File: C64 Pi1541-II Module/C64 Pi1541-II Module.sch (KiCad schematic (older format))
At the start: 28 parts, among them IC1 0.96_OLED, IC2 7406, IC3 I2C LC, J1 DC IN, J2 C64_IEC, J3 C64_IEC, J4 Faceplate, M1 Mounting, M2 Mounting, M3 Mounting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

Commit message: Changed dimensions on module
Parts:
- JP1, JP2: footprint Jumper:SolderJumper-3_P1.3mm_Open_RoundedPad1.0x1.5mm -> wire_pads:OLED_SEL
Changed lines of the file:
@@
 F 0 "JP2" V 8354 8768 50  0000 L CNN
 F 1 "P2_VCC" V 8445 8768 50  0000 L CNN
-F 2 "Jumper:SolderJumper-3_P1.3mm_Open_RoundedPad1.0x1.5mm" H 8400 8700 50  0001 C CNN
+F 2 "wire_pads:OLED_SEL" H 8400 8700 50  0001 C CNN
 F 3 "~" H 8400 8700 50  0001 C CNN
 	1    8400 8700
@@
 F 0 "JP1" V 7846 8768 50  0000 L CNN
 F 1 "P1_GND" V 7755 8768 50  0000 L CNN
-F 2 "Jumper:SolderJumper-3_P1.3mm_Open_RoundedPad1.0x1.5mm" H 7800 8700 50  0001 C CNN
+F 2 "wire_pads:OLED_SEL" H 7800 8700 50  0001 C CNN
 F 3 "~" H 7800 8700 50  0001 C CNN
 	1    7800 8700

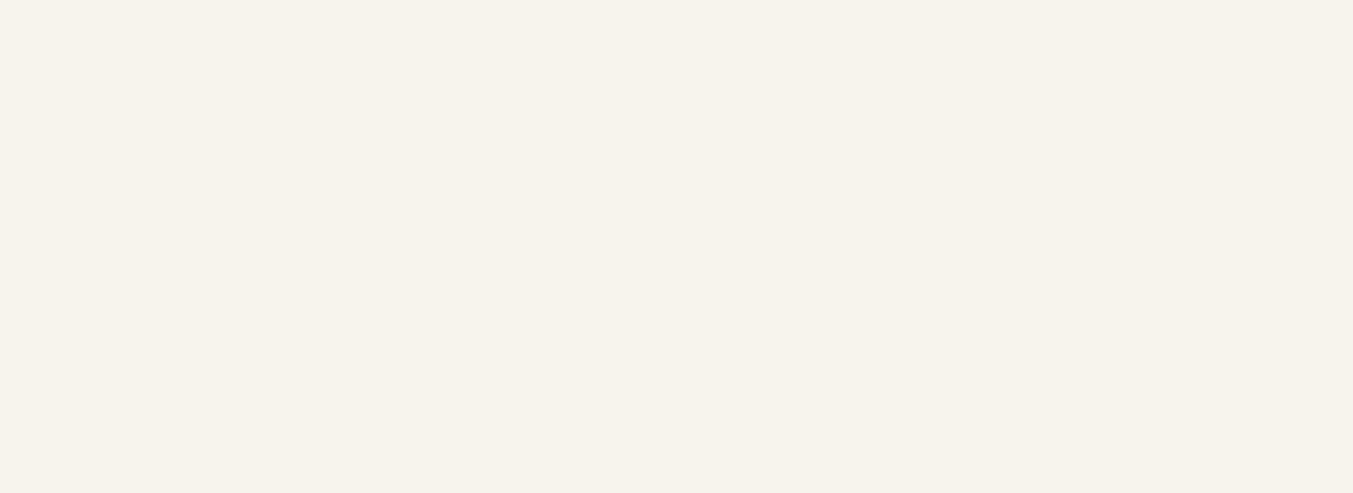
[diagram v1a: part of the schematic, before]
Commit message: Added DIN cutout
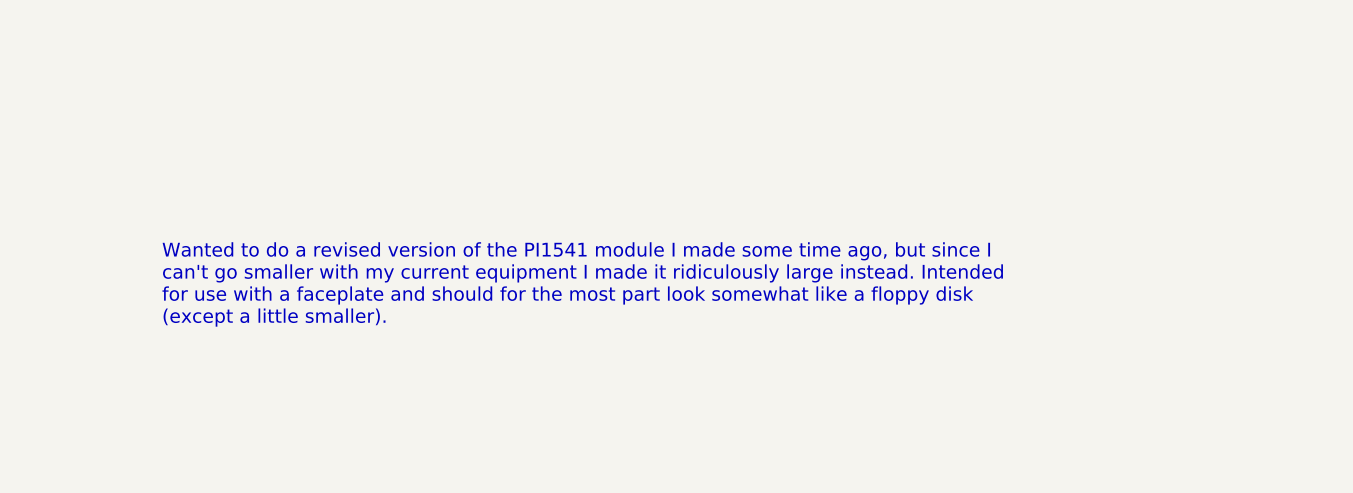
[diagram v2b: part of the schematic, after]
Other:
- note added: "Wanted to do a revised version of the PI1541 module I made some time ago, but since I\ncan't go smaller with my current equipment I made it ridiculously large instead. Intended\nfor use with a faceplate and should for the most part look somewhat like a floppy disk\n(except a little smaller)."
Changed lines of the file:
@@
 	-1   0    0    -1
 $EndComp
+Text Notes 11850 10350 0    60   ~ 0
+Wanted to do a revised version of the PI1541 module I made some time ago, but since I\ncan't go smaller with my current equipment I made it ridiculously large instead. Intended\nfor use with a faceplate and should for the most part look somewhat like a floppy disk\n(except a little smaller).
 $EndSCHEMATC

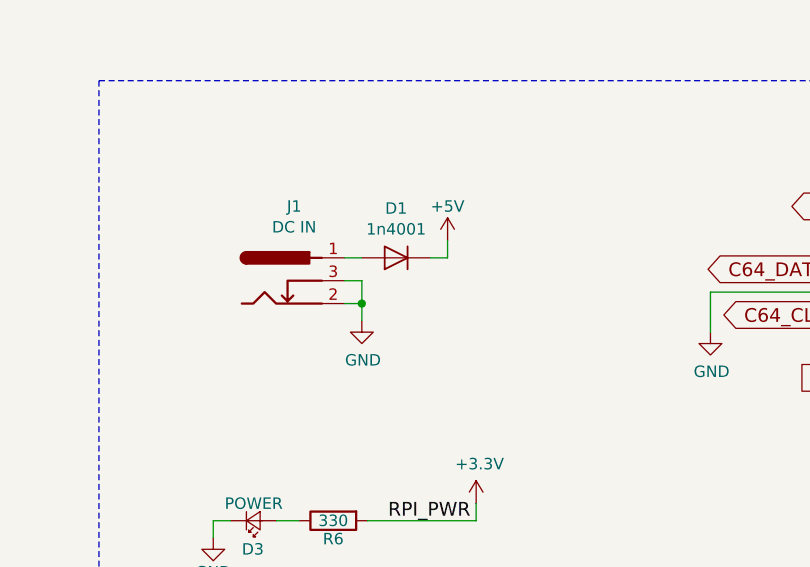
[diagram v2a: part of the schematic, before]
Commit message: Removed diode
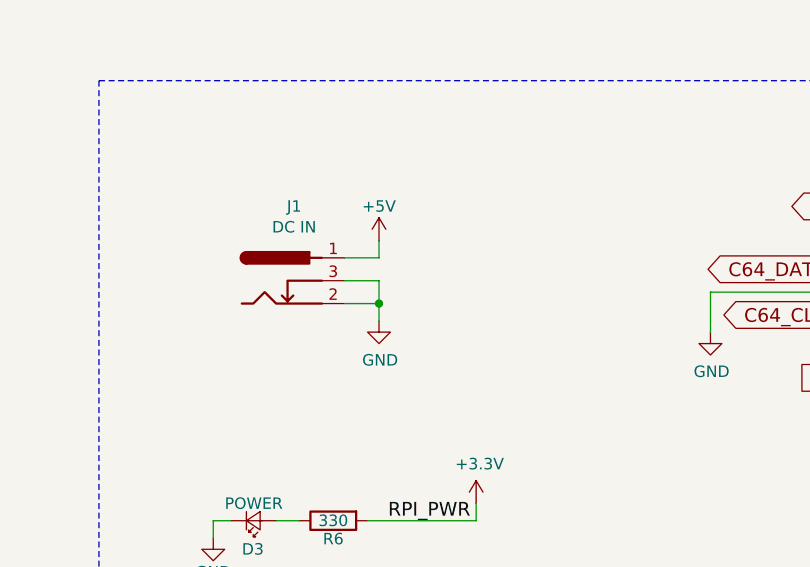
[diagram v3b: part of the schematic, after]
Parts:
- removed D1: 1n4001, Diodes_THT:D_DO-41_SOD81_P10.16mm_Horizontal, symbol barrel_jack:reverse_protect
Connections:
- net +5V: now also J1.1
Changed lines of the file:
@@
 L power:GND #PWR0101
 U 1 1 5E61DE6E
-P 2600 8850
-F 0 "#PWR0101" H 2600 8600 50  0001 C CNN
-F 1 "GND" H 2605 8677 50  0000 C CNN
-F 2 "" H 2600 8850 50  0001 C CNN
-F 3 "" H 2600 8850 50  0001 C CNN
-	1    2600 8850
-	1    0    0    -1
-$EndComp
-Wire Wire Line
-	2600 8775 2525 8775
-Wire Wire Line
-	2600 8775 2600 8675
-Wire Wire Line
-	2600 8675 2525 8675
-$Comp
-L barrel_jack:reverse_protect D1
-U 1 1 5E63055C
-P 2750 8575
-F 0 "D1" H 2750 8359 50  0000 C CNN
-F 1 "1n4001" H 2750 8450 50  0000 C CNN
-F 2 "Diodes_THT:D_DO-41_SOD81_P10.16mm_Horizontal" H 2750 8575 50  0001 C CNN
-F 3 "~" H 2750 8575 50  0001 C CNN
-	1    2750 8575
-	-1   0    0    1
-$EndComp
-Wire Wire Line
-	2525 8575 2600 8575
+P 2675 8850
+F 0 "#PWR0101" H 2675 8600 50  0001 C CNN
+F 1 "GND" H 2680 8677 50  0000 C CNN
+F 2 "" H 2675 8850 50  0001 C CNN
+F 3 "" H 2675 8850 50  0001 C CNN
+	1    2675 8850
+	1    0    0    -1
+$EndComp
+Wire Wire Line
+	2675 8775 2675 8675
 $Comp
 L power:+5V #PWR0106
 U 1 1 5E6B750D
-P 2975 8500
-F 0 "#PWR0106" H 2975 8350 50  0001 C CNN
-F 1 "+5V" H 2975 8650 50  0000 C CNN
-F 2 "" H 2975 8500 50  0001 C CNN
-F 3 "" H 2975 8500 50  0001 C CNN
-	1    2975 8500
+P 2675 8500
+F 0 "#PWR0106" H 2675 8350 50  0001 C CNN
+F 1 "+5V" H 2675 8650 50  0000 C CNN
+F 2 "" H 2675 8500 50  0001 C CNN
+F 3 "" H 2675 8500 50  0001 C CNN
+	1    2675 8500
 	1    0    0    -1
 $EndComp
@@
 	2625 9725 3100 9725
 Wire Wire Line
-	2975 8500 2975 8575
-Wire Wire Line
-	2975 8575 2900 8575
+	2675 8500 2675 8575
 $Comp
 L Switch:SW_Push SW1
@@
 $EndComp
 Wire Wire Line
-	2600 8850 2600 8775
-Connection ~ 2600 8775
+	2675 8850 2675 8775
+Connection ~ 2675 8775
 Wire Wire Line
 	2575 2450 2575 2375
@@
 	9425 9800 9425 9575
 $Comp
-L power:GND #PWR?
+L power:GND #PWR0110
 U 1 1 5F4491DA
 P 9350 10075
-F 0 "#PWR?" H 9350 9825 50  0001 C CNN
+F 0 "#PWR0110" H 9350 9825 50  0001 C CNN
 F 1 "GND" H 9355 9902 50  0000 C CNN
 F 2 "" H 9350 10075 50  0001 C CNN
@@
 $EndComp
 $Comp
-L power:+3.3V #PWR?
+L power:+3.3V #PWR0114
 U 1 1 5F44F08B
 P 9425 9575
-F 0 "#PWR?" H 9425 9425 50  0001 C CNN
+F 0 "#PWR0114" H 9425 9425 50  0001 C CNN
 F 1 "+3.3V" H 9440 9748 50  0000 C CNN
 F 2 "" H 9425 9575 50  0001 C CNN
@@
 Text Notes 11850 10350 0    60   ~ 0
 Wanted to do a revised version of the PI1541 module I made some time ago, but since I\ncan't go smaller with my current equipment I made it ridiculously large instead. Intended\nfor use with a faceplate and should for the most part look somewhat like a floppy disk\n(except a little smaller).
+Wire Wire Line
+	2525 8575 2675 8575
+Wire Wire Line
+	2525 8775 2675 8775
+Wire Wire Line
+	2525 8675 2675 8675
 $EndSCHEMATC
